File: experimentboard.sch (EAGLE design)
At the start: 172 parts, among them IC1 TL072P, IC2 LM317, IC3 LM337, IC4 TL072P, IC5 TL072P, IC6 TL072P, P1 PLR135/T9, P9 P9, U1 PCM1690, U2 DIR9001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

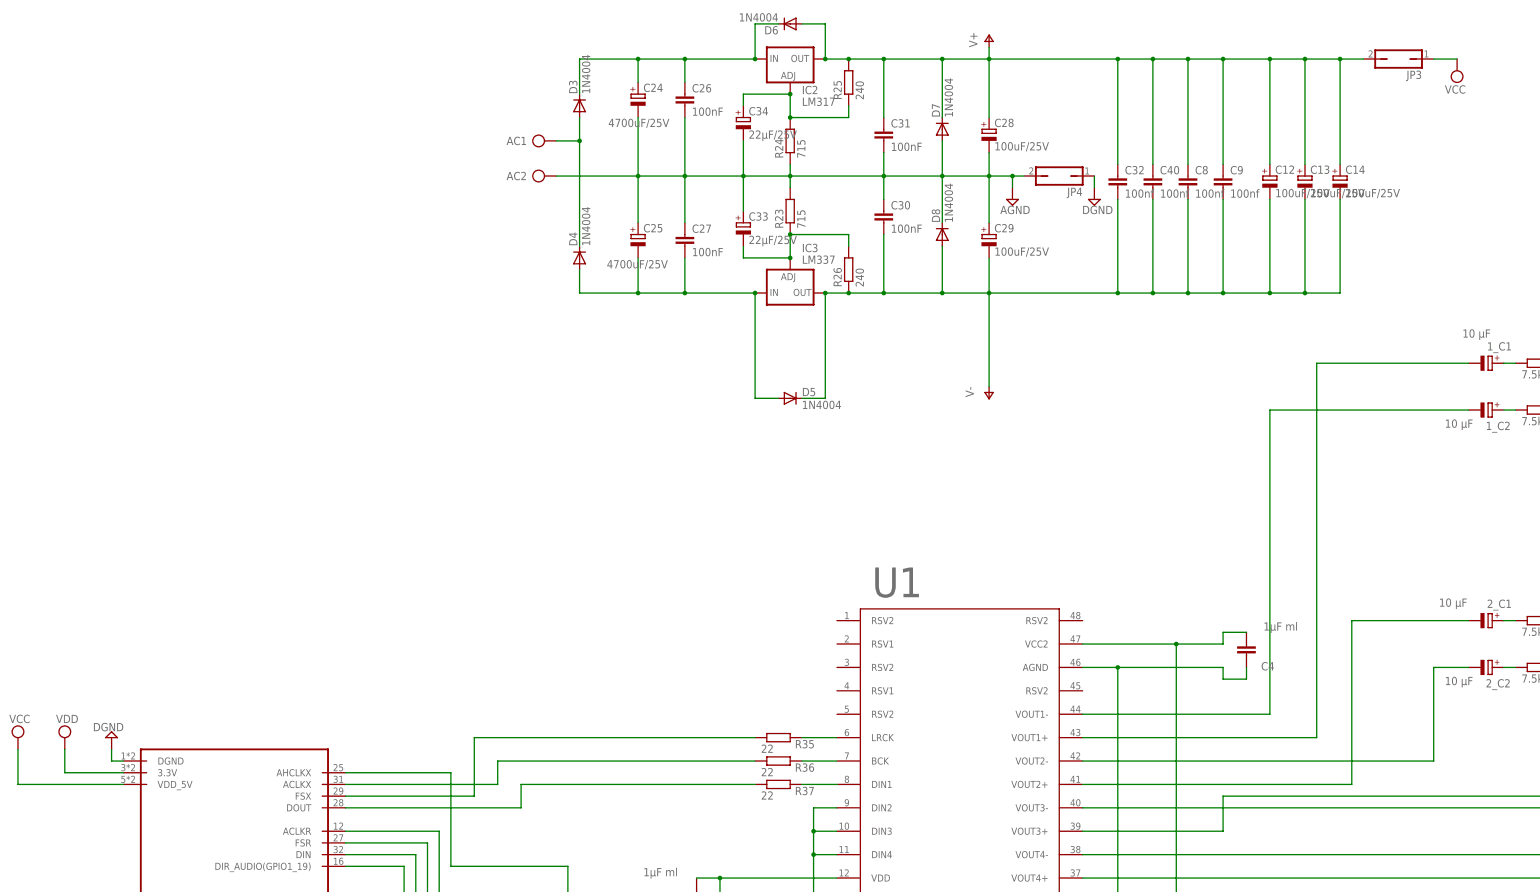
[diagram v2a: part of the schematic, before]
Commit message: Fixed bug in joining VCC and V+
I now use a 0 Ohm resistor to join VCC and V+. The jumper is also fixed,
because I had erroneously tied the PCM1690 VCC to VDD_5V on the beagle
bone, which means the beagle bone's adapter would have powered the
PCM1690.
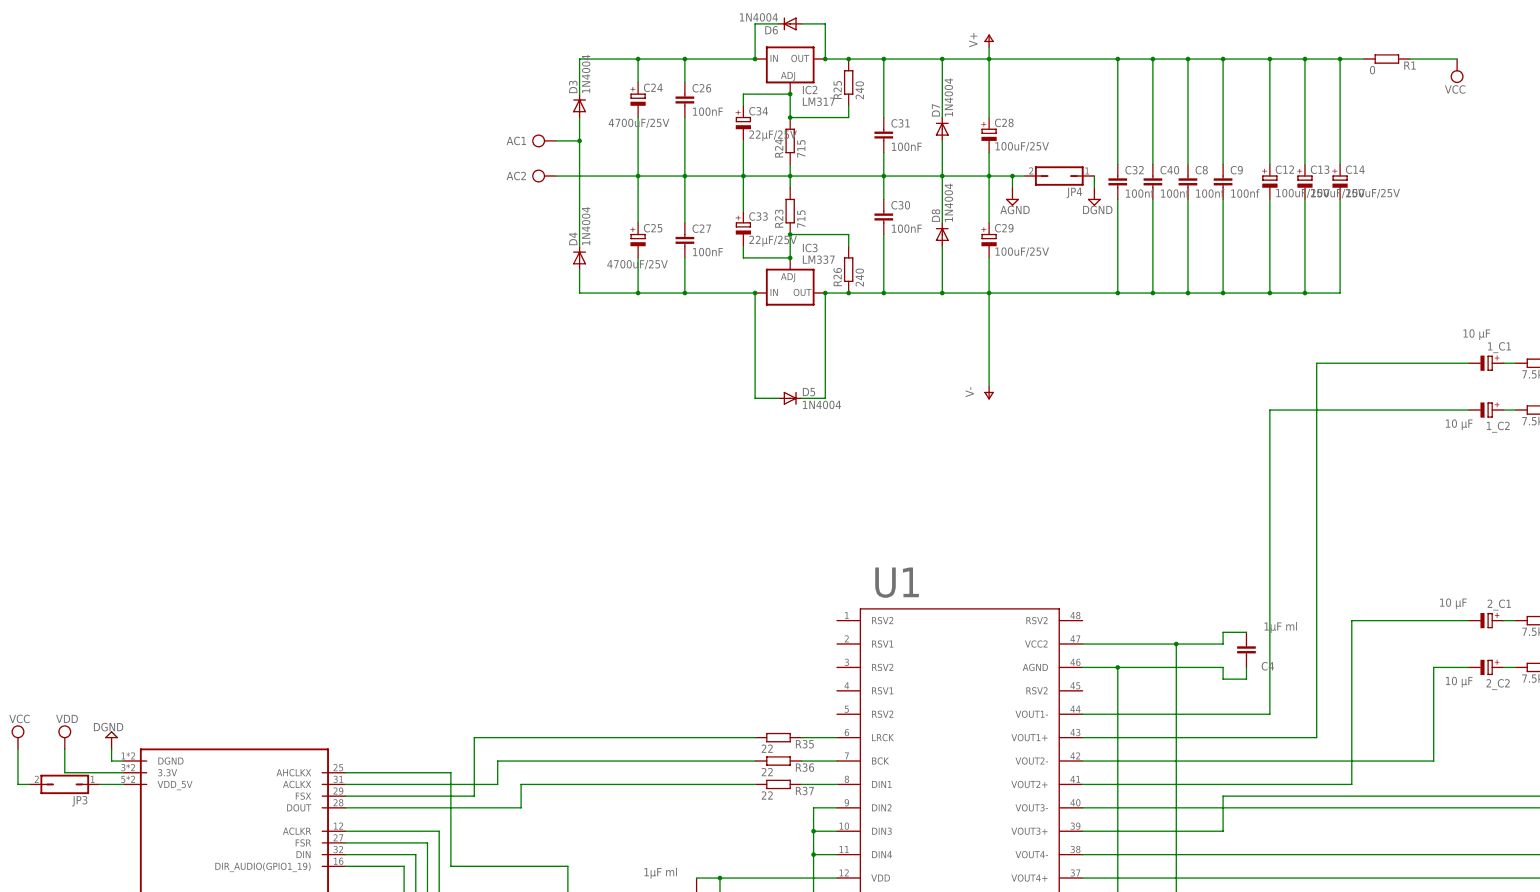
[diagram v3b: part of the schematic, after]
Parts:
- added R1: 0, rcl:R-EU_0204/2V
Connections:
- new net VDD_5V: JP3.1, P9.VDD_5V
- net V+: now also R1.1; no longer JP3.2
- net VCC: now also JP3.2, R1.2; no longer JP3.1, P9.VDD_5V
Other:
- moved on the sheet: JP3
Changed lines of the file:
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@@
 <grid distance="0.1" unitdist="inch" unit="inch" style="lines" multiple="1" display="no" altdistance="0.01" altunitdist="inch" altunit="inch"/>
 <layers>
-<layer number="1" name="Top" color="4" fill="1" visible="no" active="no"/>
-<layer number="2" name="Route2" color="1" fill="3" visible="no" active="no"/>
-<layer number="3" name="Route3" color="4" fill="3" visible="no" active="no"/>
-<layer number="14" name="Route14" color="1" fill="6" visible="no" active="no"/>
-<layer number="15" name="Route15" color="4" fill="6" visible="no" active="no"/>
-<layer number="16" name="Bottom" color="1" fill="1" visible="no" active="no"/>
-<layer number="17" name="Pads" color="2" fill="1" visible="no" active="no"/>
-<layer number="18" name="Vias" color="2" fill="1" visible="no" active="no"/>
-<layer number="19" name="Unrouted" color="6" fill="1" visible="no" active="no"/>
-<layer number="20" name="Dimension" color="15" fill="1" visible="no" active="no"/>
-<layer number="21" name="tPlace" color="7" fill="1" visible="no" active="no"/>
-<layer number="22" name="bPlace" color="7" fill="1" visible="no" active="no"/>
-<layer number="23" name="tOrigins" color="15" fill="1" visible="no" active="no"/>
-<layer number="24" name="bOrigins" color="15" fill="1" visible="no" active="no"/>
-<layer number="25" name="tNames" color="7" fill="1" visible="no" active="no"/>
-<layer number="26" name="bNames" color="7" fill="1" visible="no" active="no"/>
-<layer number="27" name="tValues" color="7" fill="1" visible="no" active="no"/>
-<layer number="28" name="bValues" color="7" fill="1" visible="no" active="no"/>
+<layer number="1" name="Top" color="4" fill="1" visible="yes" active="no"/>
+<layer number="2" name="Route2" color="1" fill="3" visible="yes" active="no"/>
+<layer number="3" name="Route3" color="4" fill="3" visible="yes" active="no"/>
+<layer number="14" name="Route14" color="1" fill="6" visible="yes" active="no"/>
+<layer number="15" name="Route15" color="4" fill="6" visible="yes" active="no"/>
+<layer number="16" name="Bottom" color="1" fill="1" visible="yes" active="no"/>
+<layer number="17" name="Pads" color="2" fill="1" visible="yes" active="no"/>
+<layer number="18" name="Vias" color="2" fill="1" visible="yes" active="no"/>
+<layer number="19" name="Unrouted" color="6" fill="1" visible="yes" active="no"/>
+<layer number="20" name="Dimension" color="15" fill="1" visible="yes" active="no"/>
+<layer number="21" name="tPlace" color="7" fill="1" visible="yes" active="no"/>
+<layer number="22" name="bPlace" color="7" fill="1" visible="yes" active="no"/>
+<layer number="23" name="tOrigins" color="15" fill="1" visible="yes" active="no"/>
+<layer number="24" name="bOrigins" color="15" fill="1" visible="yes" active="no"/>
+<layer number="25" name="tNames" color="7" fill="1" visible="yes" active="no"/>
+<layer number="26" name="bNames" color="7" fill="1" visible="yes" active="no"/>
+<layer number="27" name="tValues" color="7" fill="1" visible="yes" active="no"/>
+<layer number="28" name="bValues" color="7" fill="1" visible="yes" active="no"/>
 <layer number="29" name="tStop" color="7" fill="3" visible="no" active="no"/>
 <layer number="30" name="bStop" color="7" fill="6" visible="no" active="no"/>
@@
 <layer number="35" name="tGlue" color="7" fill="4" visible="no" active="no"/>
 <layer number="36" name="bGlue" color="7" fill="5" visible="no" active="no"/>
-<layer number="37" name="tTest" color="7" fill="1" visible="no" active="no"/>
-<layer number="38" name="bTest" color="7" fill="1" visible="no" active="no"/>
+<layer number="37" name="tTest" color="7" fill="1" visible="yes" active="no"/>
+<layer number="38" name="bTest" color="7" fill="1" visible="yes" active="no"/>
 <layer number="39" name="tKeepout" color="4" fill="11" visible="no" active="no"/>
 <layer number="40" name="bKeepout" color="1" fill="11" visible="no" active="no"/>
@@
 <layer number="44" name="Drills" color="7" fill="1" visible="no" active="no"/>
 <layer number="45" name="Holes" color="7" fill="1" visible="no" active="no"/>
-<layer number="46" name="Milling" color="3" fill="1" visible="no" active="no"/>
-<layer number="47" name="Measures" color="7" fill="1" visible="no" active="no"/>
-<layer number="48" name="Document" color="7" fill="1" visible="no" active="no"/>
-<layer number="49" name="Reference" color="7" fill="1" visible="no" active="no"/>
-<layer number="51" name="tDocu" color="7" fill="1" visible="no" active="no"/>
-<layer number="52" name="bDocu" color="7" fill="1" visible="no" active="no"/>
+<layer number="46" name="Milling" color="3" fill="1" visible="yes" active="no"/>
+<layer number="47" name="Measures" color="7" fill="1" visible="yes" active="no"/>
+<layer number="48" name="Document" color="7" fill="1" visible="yes" active="no"/>
+<layer number="49" name="Reference" color="7" fill="1" visible="yes" active="no"/>
+<layer number="51" name="tDocu" color="7" fill="1" visible="yes" active="no"/>
+<layer number="52" name="bDocu" color="7" fill="1" visible="yes" active="no"/>
 <layer number="90" name="Modules" color="5" fill="1" visible="yes" active="yes"/>
 <layer number="91" name="Nets" color="2" fill="1" visible="yes" active="yes"/>
@@
 <part name="SUPPLY11" library="supply2" deviceset="DGND" device=""/>
 <part name="SUPPLY12" library="supply2" deviceset="DGND" device=""/>
+<part name="R1" library="rcl" deviceset="R-EU_" device="0204/2V" value="0"/>
 </parts>
 <sheets>
@@
 <instance part="C13" gate="G$1" x="177.8" y="215.9"/>
 <instance part="C14" gate="G$1" x="185.42" y="215.9"/>
-<instance part="JP3" gate="A" x="198.12" y="241.3" rot="R90"/>
+<instance part="JP3" gate="A" x="-91.44" y="83.82" rot="R90"/>
 <instance part="C16" gate="G$1" x="96.52" y="-187.96" rot="R90"/>
 <instance part="JP4" gate="A" x="124.46" y="215.9" rot="R90"/>
@@
 <instance part="SUPPLY11" gate="G$1" x="152.4" y="-124.46"/>
 <instance part="SUPPLY12" gate="G$1" x="172.72" y="-124.46"/>
+<instance part="R1" gate="G$1" x="195.58" y="241.3" smashed="yes">
+<attribute name="NAME" x="199.136" y="238.9886" size="1.778" layer="95"/>
+<attribute name="VALUE" x="191.77" y="237.998" size="1.778" layer="96"/>
+</instance>
 </instances>
 <busses>
@@
 </segment>
 <segment>
-<pinref part="P9" gate="G$1" pin="VDD_5V"/>
 <pinref part="SUPPLY28" gate="G$1" pin="VCC"/>
-<wire x1="-78.74" y1="83.82" x2="-101.6" y2="83.82" width="0.1524" layer="91"/>
 <wire x1="-101.6" y1="83.82" x2="-101.6" y2="91.44" width="0.1524" layer="91"/>
-</segment>
-<segment>
-<pinref part="JP3" gate="A" pin="1"/>
+<pinref part="JP3" gate="A" pin="2"/>
+<wire x1="-99.06" y1="83.82" x2="-101.6" y2="83.82" width="0.1524" layer="91"/>
+</segment>
+<segment>
 <pinref part="SUPPLY27" gate="G$1" pin="VCC"/>
-<wire x1="205.74" y1="241.3" x2="210.82" y2="241.3" width="0.1524" layer="91"/>
+<pinref part="R1" gate="G$1" pin="2"/>
+<wire x1="200.66" y1="241.3" x2="210.82" y2="241.3" width="0.1524" layer="91"/>
 </segment>
 </net>
@@
 <pinref part="C14" gate="G$1" pin="+"/>
 <wire x1="185.42" y1="218.44" x2="185.42" y2="241.3" width="0.1524" layer="91"/>
-<pinref part="JP3" gate="A" pin="2"/>
-<wire x1="185.42" y1="241.3" x2="190.5" y2="241.3" width="0.1524" layer="91"/>
+<pinref part="R1" gate="G$1" pin="1"/>
+<wire x1="190.5" y1="241.3" x2="185.42" y2="241.3" width="0.1524" layer="91"/>
 <junction x="185.42" y="241.3"/>
 </segment>
@@
 </segment>
 </net>
+<net name="VDD_5V" class="0">
+<segment>
+<pinref part="P9" gate="G$1" pin="VDD_5V"/>
+<pinref part="JP3" gate="A" pin="1"/>
+<wire x1="-78.74" y1="83.82" x2="-83.82" y2="83.82" width="0.1524" layer="91"/>
+</segment>
+</net>
